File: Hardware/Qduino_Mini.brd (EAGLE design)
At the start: 38.1 x 25.4 mm, 45 parts, among them Q1 PFET, U1 ATMEGA32U41:1-LESS_PASTE, U2 MCP73831, U3 MAX17048, U4 TPS78233, U5 MIGHTYQ-L-SILK, U6 MIGHTYQ-S-SILK, U7 DNP, Y1 8MHZ

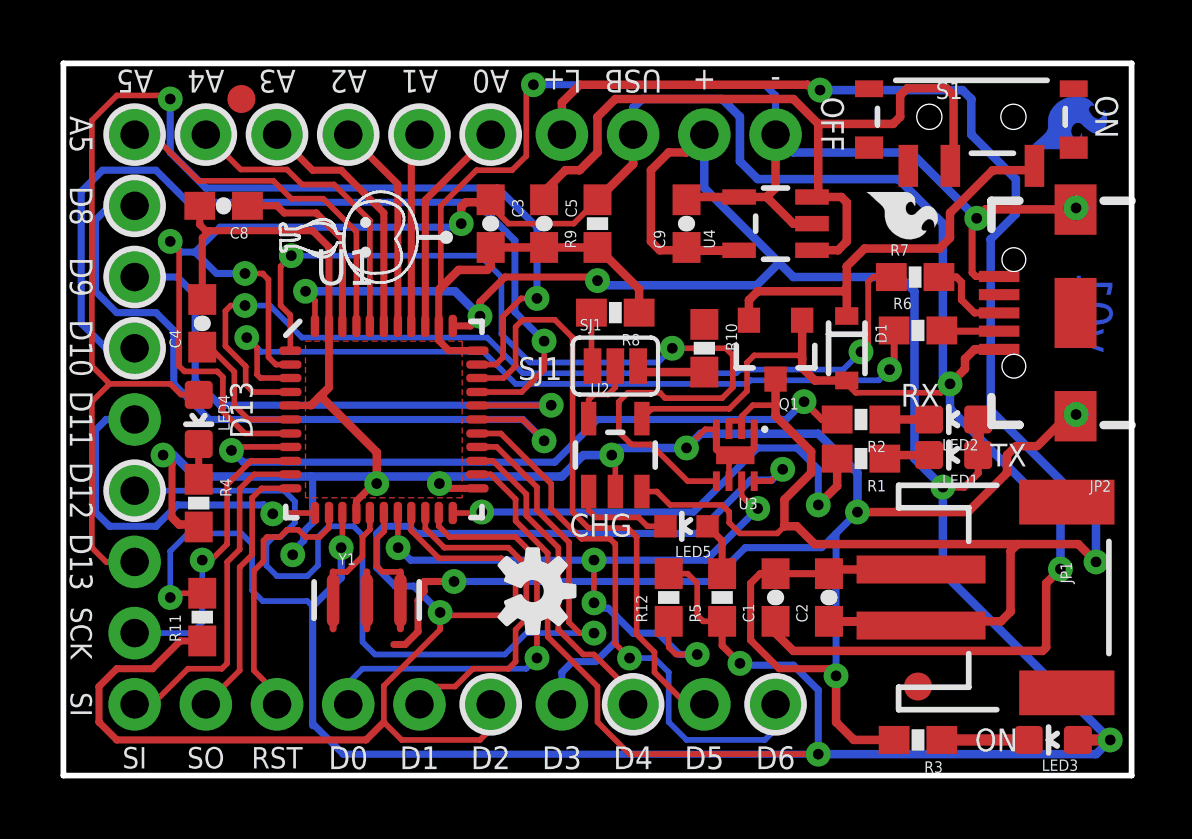
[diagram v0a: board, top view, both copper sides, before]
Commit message: testing out a reduced sized die pad to provide the recommended mechanical support, but with low pad to pin short likelihood
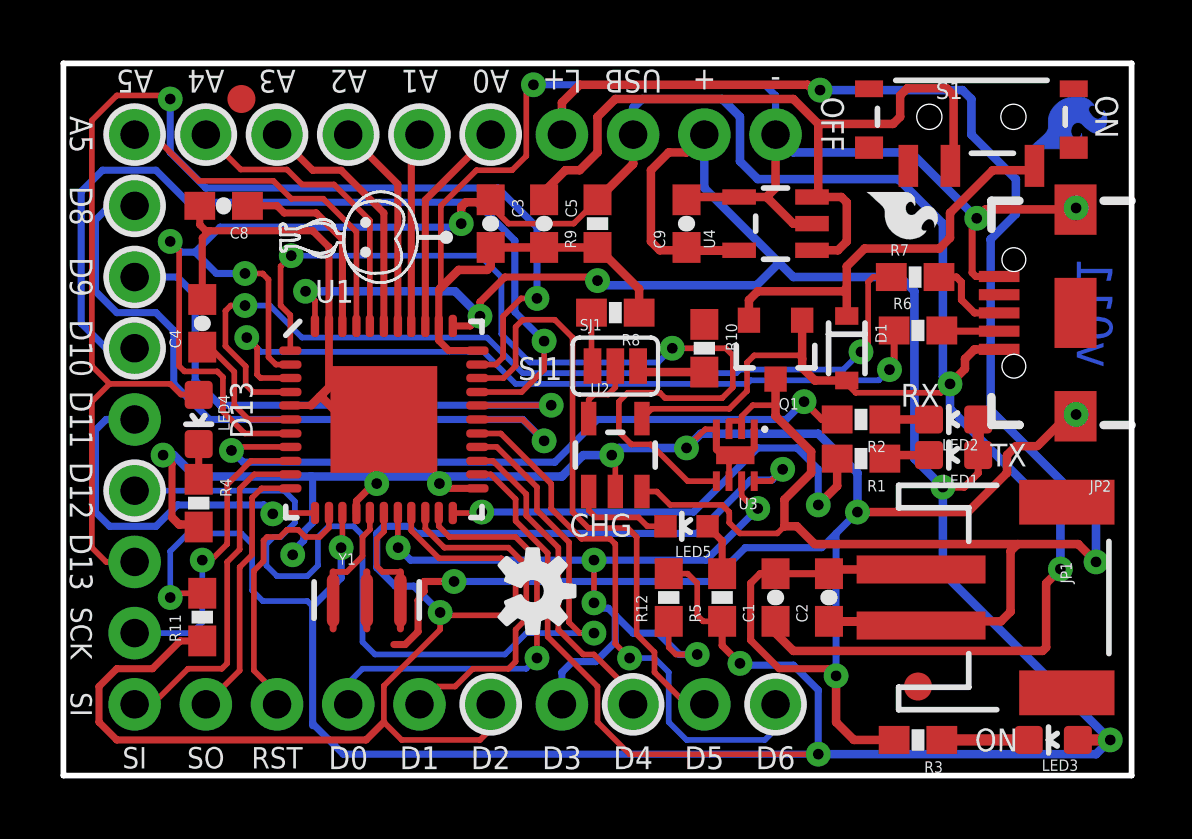
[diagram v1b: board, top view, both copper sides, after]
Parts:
- U1: value ATMEGA32U41:1-LESS_PASTE -> ATMEGA32U4QFN-44-PROD-OPTIMIZED; device SparkFun-DigitalIC:QFN-44-NOPAD_1:1-LESS_PASTE -> Testing:QFN-44-PROD-OPTIMIZED
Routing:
- removed copper zone on layer 1, net N$3
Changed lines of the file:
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@@
 <attributes>
 <attribute name="DESIGNER" value="Quin from Qtechknow"/>
-<attribute name="VERSION" value="v01"/>
+<attribute name="VERSION" value="v011"/>
 </attributes>
 <variantdefs>
@@
 <attribute name="PROD_ID" value="CONN-11443" x="34.29" y="6.35" size="1.778" layer="27" rot="R270" display="off"/>
 </element>
-<element name="U1" library="SparkFun-DigitalIC" package="QFN-44-NOPAD_1:1-LESS_PASTE" value="ATMEGA32U41:1-LESS_PASTE" x="11.43" y="12.7">
+<element name="U1" library="Testing" package="QFN-44-PROD-OPTIMIZED" value="ATMEGA32U4QFN-44-PROD-OPTIMIZED" x="11.43" y="12.7">
 <attribute name="PROD_ID" value="IC-10828" x="11.43" y="12.7" size="1.778" layer="27" display="off"/>
 </element>
@@
 <wire x1="18.835" y1="14.6422" x2="18.8722" y2="14.605" width="0.2032" layer="1"/>
 </signal>
-<signal name="N$3">
-<polygon width="0" layer="1" pour="cutout">
-<vertex x="8.636" y="15.1384"/>
-<vertex x="8.636" y="15.494"/>
-<vertex x="8.9408" y="15.494"/>
-<vertex x="14.224" y="15.494"/>
-<vertex x="14.224" y="9.9568"/>
-<vertex x="14.224" y="9.906"/>
-<vertex x="8.636" y="9.906"/>
-</polygon>
-</signal>
 </signals>

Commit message: Rerouted grounds under IC
Cleaned the ground traces under IC up. Passes DRC now too.
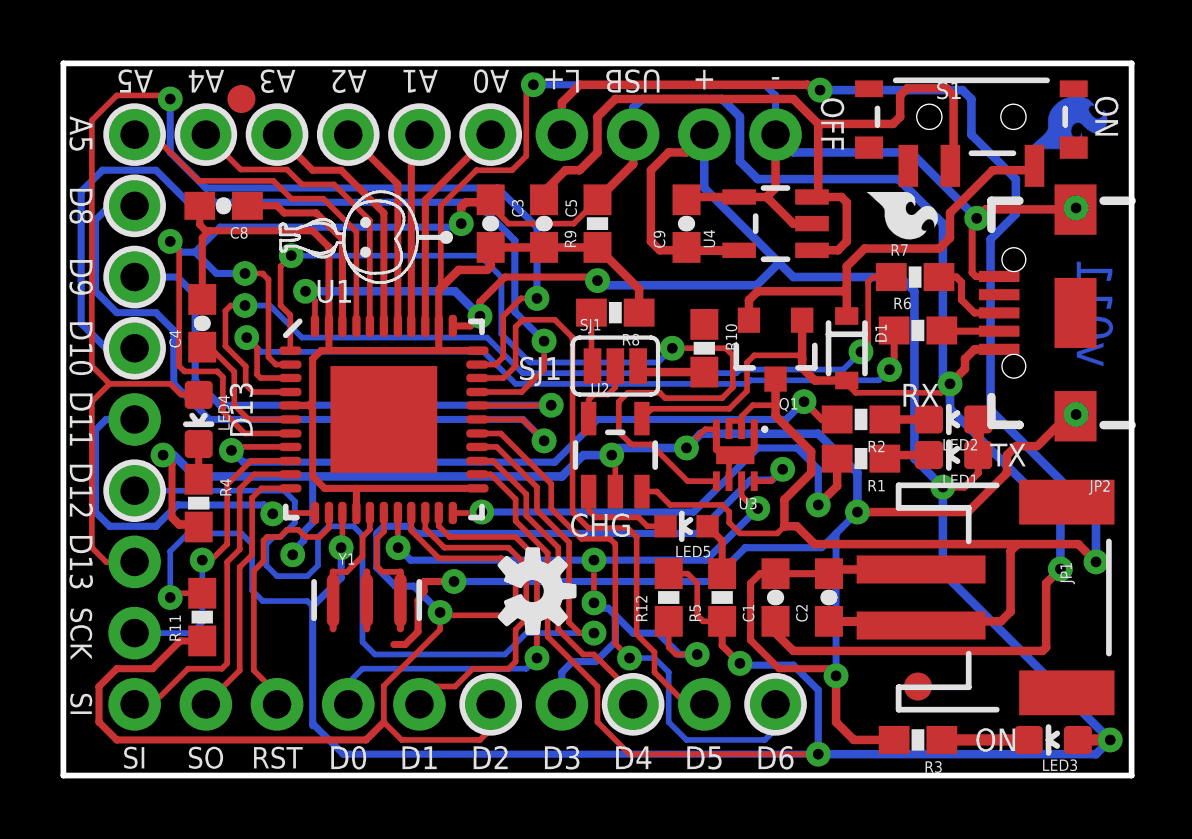
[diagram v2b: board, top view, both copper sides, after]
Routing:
- net GND: track 168.4 -> 174.4 mm, vias 13 -> 11
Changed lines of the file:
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@@
 <?xml version="1.0" encoding="utf-8"?>
 <!DOCTYPE eagle SYSTEM "eagle.dtd">
-<eagle version="7.2.0">
+<eagle version="7.1.0">
 <drawing>
 <settings>
@@
 <setting verticaltext="up"/>
 </settings>
-<grid distance="0.05" unitdist="inch" unit="inch" style="lines" multiple="1" display="yes" altdistance="0.25" altunitdist="mil" altunit="mil"/>
+<grid distance="0.05" unitdist="inch" unit="inch" style="lines" multiple="1" display="yes" altdistance="0.005" altunitdist="inch" altunit="inch"/>
 <layers>
 <layer number="1" name="Top" color="4" fill="1" visible="yes" active="yes"/>
@@
 <layer number="47" name="Measures" color="7" fill="1" visible="no" active="yes"/>
 <layer number="48" name="Document" color="7" fill="1" visible="no" active="yes"/>
-<layer number="49" name="Reference" color="7" fill="1" visible="yes" active="yes"/>
+<layer number="49" name="Reference" color="7" fill="1" visible="no" active="yes"/>
 <layer number="50" name="dxf" color="7" fill="1" visible="no" active="no"/>
 <layer number="51" name="tDocu" color="6" fill="1" visible="yes" active="yes"/>
@@
 <wire x1="27.559" y1="8.636" x2="28.321" y2="9.398" width="0.254" layer="16"/>
 <wire x1="4.699" y1="10.668" x2="8.8265" y2="10.668" width="0.3048" layer="16"/>
-<wire x1="8.8265" y1="10.668" x2="10.9728" y2="10.668" width="0.3048" layer="16"/>
-<wire x1="10.9728" y1="10.668" x2="13.4112" y2="10.668" width="0.3048" layer="16"/>
-<wire x1="13.4112" y1="10.668" x2="17.78" y2="10.668" width="0.3048" layer="16"/>
+<wire x1="8.8265" y1="10.668" x2="17.78" y2="10.668" width="0.3048" layer="16"/>
 <wire x1="32.258" y1="9.398" x2="33.655" y2="10.795" width="0.3048" layer="1"/>
 <wire x1="17.78" y1="10.668" x2="18.542" y2="11.43" width="0.3048" layer="16"/>
@@
 <wire x1="13.43" y1="17.367" x2="13.387734375" y2="17.324734375" width="0.254" layer="1"/>
 <wire x1="13.387734375" y1="17.324734375" x2="13.387734375" y2="16.0365" width="0.254" layer="1"/>
-<wire x1="13.387734375" y1="16.0365" x2="13.387734375" y2="15.517465625" width="0.254" layer="1"/>
-<wire x1="13.387734375" y1="15.517465625" x2="13.747465625" y2="15.157734375" width="0.254" layer="1"/>
-<wire x1="13.747465625" y1="15.157734375" x2="14.7665" y2="15.157734375" width="0.254" layer="1"/>
-<wire x1="9.472265625" y1="16.0365" x2="9.472265625" y2="13.841065625" width="0.2794" layer="1"/>
-<wire x1="9.472265625" y1="13.841065625" x2="9.144" y2="13.5128" width="0.3048" layer="1"/>
-<wire x1="8.8312" y1="13.2" x2="8.0935" y2="13.2" width="0.254" layer="1"/>
-<wire x1="14.7665" y1="10.242265625" x2="13.582934375" y2="10.242265625" width="0.254" layer="1"/>
-<wire x1="13.582934375" y1="10.242265625" x2="13.4112" y2="10.414" width="0.254" layer="1"/>
-<via x="13.4112" y="10.414" extent="1-16" drill="0.381"/>
-<wire x1="13.3604" y1="10.6172" x2="13.4112" y2="10.668" width="0.254" layer="16"/>
-<wire x1="10.451134375" y1="9.3635" x2="10.451134375" y2="9.790734375" width="0.254" layer="1"/>
-<via x="11.176" y="10.414" extent="1-16" drill="0.381"/>
-<wire x1="10.9728" y1="10.2616" x2="10.9728" y2="10.668" width="0.254" layer="16"/>
-<wire x1="10.451134375" y1="9.790734375" x2="11.0744" y2="10.414" width="0.254" layer="1"/>
-<wire x1="11.0744" y1="10.414" x2="11.176" y2="10.414" width="0.254" layer="1"/>
-<wire x1="8.8312" y1="13.2" x2="9.144" y2="13.5128" width="0.3048" layer="1"/>
-<wire x1="9.144" y1="13.5128" x2="9.1948" y2="13.5128" width="0.254" layer="1"/>
-<wire x1="9.1948" y1="13.5128" x2="11.176" y2="11.5316" width="0.3048" layer="1"/>
-<wire x1="11.176" y1="11.5316" x2="11.176" y2="10.414" width="0.3048" layer="1"/>
-<wire x1="11.176" y1="10.414" x2="11.0236" y2="10.2616" width="0.254" layer="16"/>
-<wire x1="11.0236" y1="10.2616" x2="10.9728" y2="10.2616" width="0.254" layer="16"/>
-<wire x1="13.3604" y1="10.6172" x2="13.4112" y2="10.5664" width="0.254" layer="16"/>
-<wire x1="13.4112" y1="10.5664" x2="13.4112" y2="10.414" width="0.254" layer="16"/>
+<wire x1="13.387734375" y1="16.0365" x2="13.387734375" y2="15.157734375" width="0.254" layer="1"/>
 <wire x1="3.556" y1="11.43" x2="3.8735" y2="11.1125" width="0.254" layer="1"/>
 <wire x1="3.8735" y1="11.1125" x2="3.8735" y2="9.2075" width="0.254" layer="1"/>
@@
 <via x="36.1188" y="12.8778" extent="1-16" drill="0.381"/>
 <wire x1="36.1188" y1="20.193" x2="36.1188" y2="20.2438" width="0.3048" layer="1"/>
+<wire x1="9.472265625" y1="16.0365" x2="9.472265625" y2="15.157734375" width="0.254" layer="1"/>
+<wire x1="8.0935" y1="13.2" x2="8.763" y2="13.2" width="0.254" layer="1"/>
+<wire x1="9.315734375" y1="10.242265625" x2="8.89" y2="10.668" width="0.254" layer="1"/>
+<wire x1="8.89" y1="10.668" x2="8.89" y2="13.073" width="0.254" layer="1"/>
+<wire x1="8.89" y1="13.073" x2="8.763" y2="13.2" width="0.254" layer="1"/>
+<wire x1="8.763" y1="13.2" x2="8.89" y2="13.327" width="0.254" layer="1"/>
+<wire x1="8.89" y1="13.327" x2="8.89" y2="14.859" width="0.254" layer="1"/>
+<wire x1="8.89" y1="14.859" x2="9.188734375" y2="15.157734375" width="0.254" layer="1"/>
+<wire x1="14.7665" y1="10.242265625" x2="10.451134375" y2="10.242265625" width="0.254" layer="1"/>
+<wire x1="10.451134375" y1="10.242265625" x2="9.315734375" y2="10.242265625" width="0.254" layer="1"/>
+<wire x1="10.451134375" y1="9.3635" x2="10.451134375" y2="10.242265625" width="0.254" layer="1"/>
+<wire x1="14.7665" y1="15.157734375" x2="13.387734375" y2="15.157734375" width="0.254" layer="1"/>
+<wire x1="13.387734375" y1="15.157734375" x2="9.525" y2="15.157734375" width="0.254" layer="1"/>
+<wire x1="9.472265625" y1="15.157734375" x2="9.188734375" y2="15.157734375" width="0.254" layer="1"/>
+<wire x1="9.472265625" y1="15.157734375" x2="9.525" y2="15.157734375" width="0.254" layer="1"/>
 </signal>
 <signal name="RST">

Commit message: Used version of MCP73831 in current library, rather than legacy library. No real change.
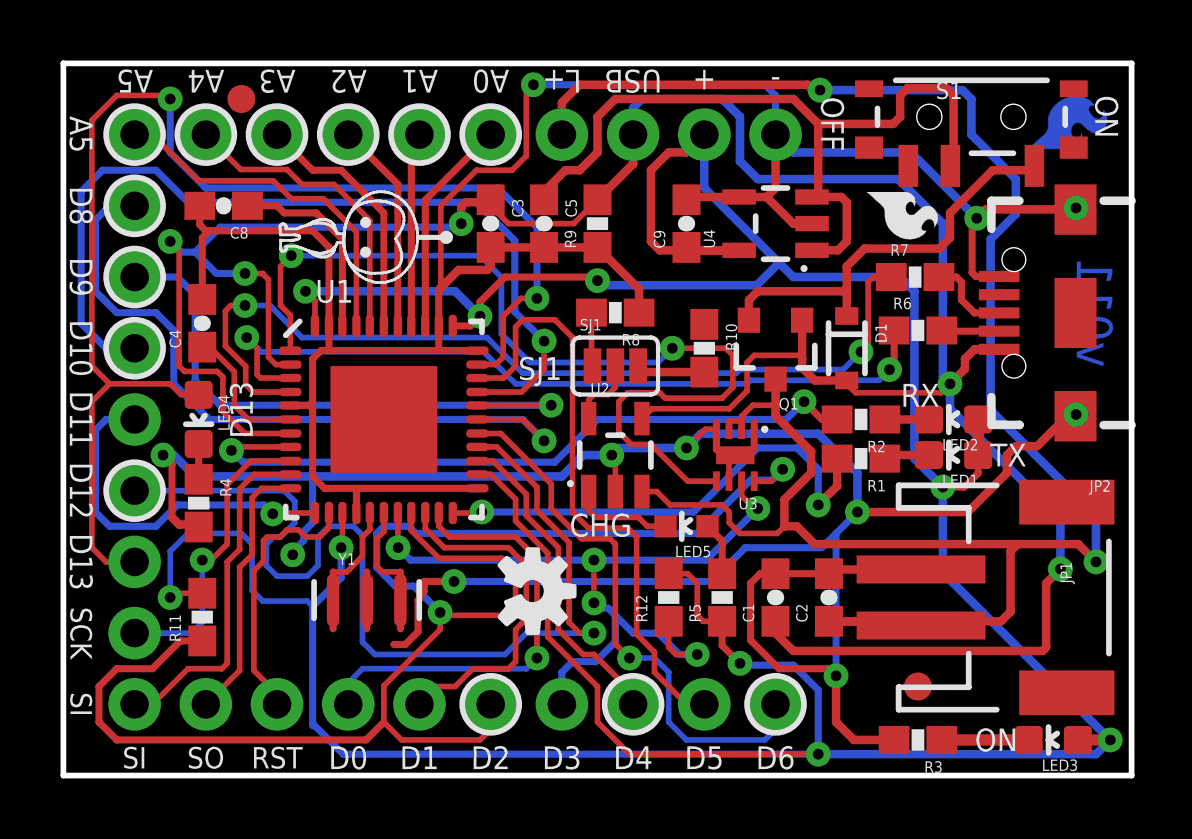
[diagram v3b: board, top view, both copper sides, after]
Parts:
- U2: device SparkFun:SOT23-5 -> SparkFun-PowerIC:SOT23-5
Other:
- board text added: "D"
- board text added: "G"
- board text added: "S"
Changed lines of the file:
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@@
 <?xml version="1.0" encoding="utf-8"?>
 <!DOCTYPE eagle SYSTEM "eagle.dtd">
-<eagle version="7.1.0">
+<eagle version="7.2.0">
 <drawing>
 <settings>
@@
 <setting verticaltext="up"/>
 </settings>
-<grid distance="0.05" unitdist="inch" unit="inch" style="lines" multiple="1" display="yes" altdistance="0.005" altunitdist="inch" altunit="inch"/>
+<grid distance="0.005" unitdist="inch" unit="inch" style="lines" multiple="1" display="yes" altdistance="0.005" altunitdist="inch" altunit="inch"/>
 <layers>
 <layer number="1" name="Top" color="4" fill="1" visible="yes" active="yes"/>
@@
 <text x="17.0053" y="14.5161" size="0.8128" layer="21" ratio="16" rot="SR0" align="center">SJ1</text>
 <text x="-4.1148" y="-11.8364" size="1.778" layer="51">Revised by: Brent Wilkins</text>
+<text x="26.797" y="16.51" size="0.8128" layer="51" font="vector">G</text>
+<text x="23.368" y="16.383" size="0.8128" layer="51" font="vector">S</text>
+<text x="24.257" y="13.208" size="0.8128" layer="51" font="vector">D</text>
 </plain>
 <attributes>
@@
 <attribute name="PROD_ID" value="DIO-00819" x="22.225" y="8.89" size="1.778" layer="27" rot="R90" display="off"/>
 </element>
-<element name="U2" library="SparkFun" package="SOT23-5" value="MCP73831" x="19.685" y="11.43">
+<element name="U2" library="SparkFun-PowerIC" package="SOT23-5" value="MCP73831" x="19.685" y="11.43">
 <attribute name="PROD_ID" value="IC-09995" x="19.685" y="11.43" size="1.778" layer="27" display="off"/>
 </element>
@@
 <wire x1="29.63" y1="1.27" x2="28.194" y2="1.27" width="0.3048" layer="1"/>
 <wire x1="28.194" y1="1.27" x2="27.559" y2="1.905" width="0.3048" layer="1"/>
-<wire x1="27.559" y1="1.905" x2="27.559" y2="3.556" width="0.3048" layer="1"/>
 <wire x1="4.1275" y1="8.9535" x2="3.8735" y2="9.2075" width="0.3048" layer="1"/>
 <wire x1="33.655" y1="10.795" x2="33.655" y2="11.43" width="0.3048" layer="1"/>
@@
 <wire x1="13.387734375" y1="15.157734375" x2="9.525" y2="15.157734375" width="0.254" layer="1"/>
 <wire x1="9.472265625" y1="15.157734375" x2="9.188734375" y2="15.157734375" width="0.254" layer="1"/>
+<wire x1="27.559" y1="1.905" x2="27.559" y2="3.556" width="0.3048" layer="1"/>
 <wire x1="9.472265625" y1="15.157734375" x2="9.525" y2="15.157734375" width="0.254" layer="1"/>
 </signal>
@@
 <contactref element="C9" pad="1"/>
 <wire x1="32.627" y1="12.7" x2="32.627" y2="11.43" width="0.4064" layer="1"/>
-<wire x1="36.183" y1="1.27" x2="37.338" y2="1.27" width="0.4064" layer="1"/>
 <via x="37.338" y="1.27" extent="1-16" drill="0.381"/>
 <via x="31.369" y="10.287" extent="1-16" drill="0.381"/>
@@
 <wire x1="16.129" y1="9.0805" x2="17.272" y2="7.9375" width="0.2032" layer="1"/>
 <wire x1="17.272" y1="7.9375" x2="17.272" y2="4.953" width="0.2032" layer="1"/>
-<wire x1="26.924" y1="0.762" x2="26.924" y2="3.048" width="0.254" layer="16"/>
 <wire x1="31.369" y1="10.287" x2="31.369" y2="7.239" width="0.3048" layer="16"/>
 <wire x1="24.0999" y1="18.735" x2="22.325" y2="18.735" width="0.3048" layer="1"/>
@@
 <wire x1="32.131" y1="10.287" x2="32.627" y2="10.783" width="0.254" layer="1"/>
 <wire x1="32.627" y1="10.783" x2="32.627" y2="11.43" width="0.254" layer="1"/>
+<wire x1="26.924" y1="0.762" x2="26.924" y2="3.048" width="0.254" layer="16"/>
+<wire x1="36.183" y1="1.27" x2="37.338" y2="1.27" width="0.4064" layer="1"/>
 </signal>
 <signal name="UD-">
